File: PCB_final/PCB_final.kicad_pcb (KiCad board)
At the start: 4 copper layers, 90 x 95 mm, 115 parts, among them J1 02x30_Shift_Register_Connector, J2 02x30_ADC_Connector, J3 PicoPinSocketB, J4 PicoPinSocketA, U1 74HC595, U10 MCP6001T-I_OT, U2 74HC595, U3 74HC595, U4 74HC595, U5 74HC595, U6 74HC595, U7 74HC595, U8 MAX11643EEG, U9 MAX11643EEG

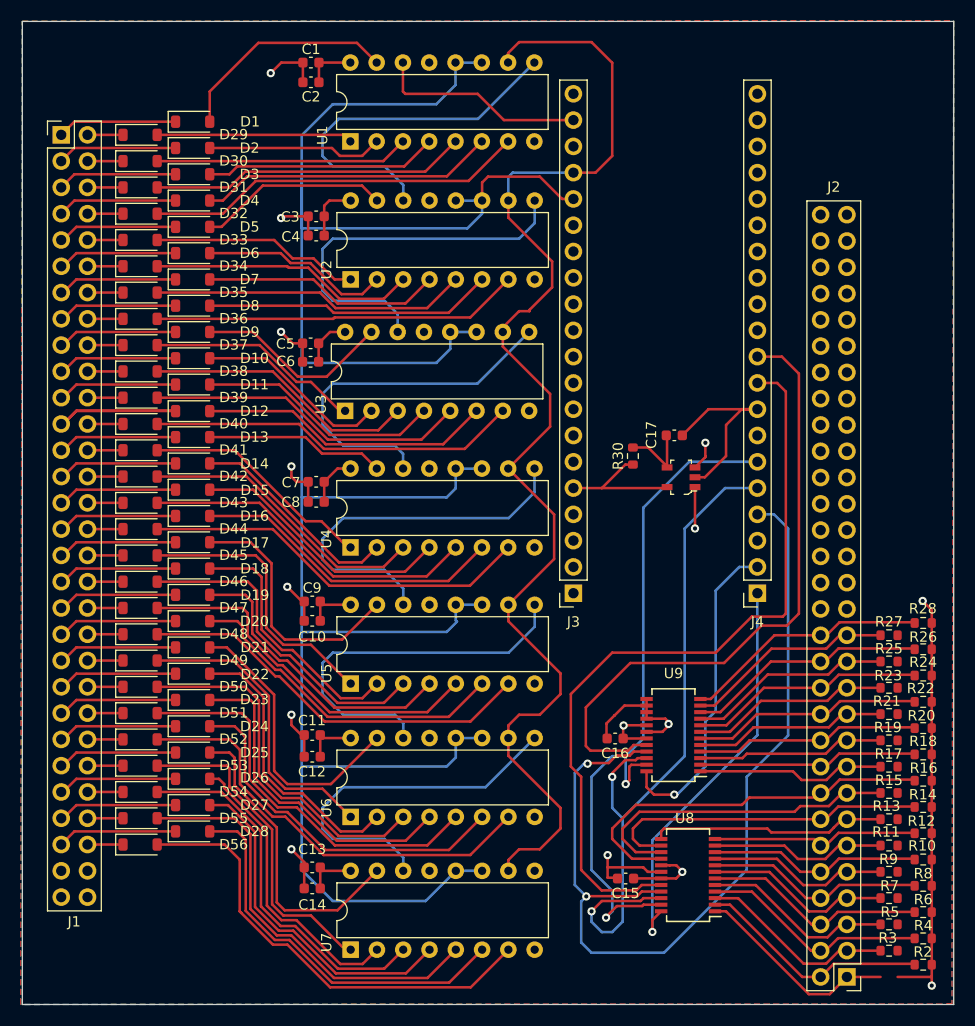
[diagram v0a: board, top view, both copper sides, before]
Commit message: Found naming errors with schematic and a few traces in PCB that weren't connected correctly. PCB now passes DRC with only a few warnings about silkscreen
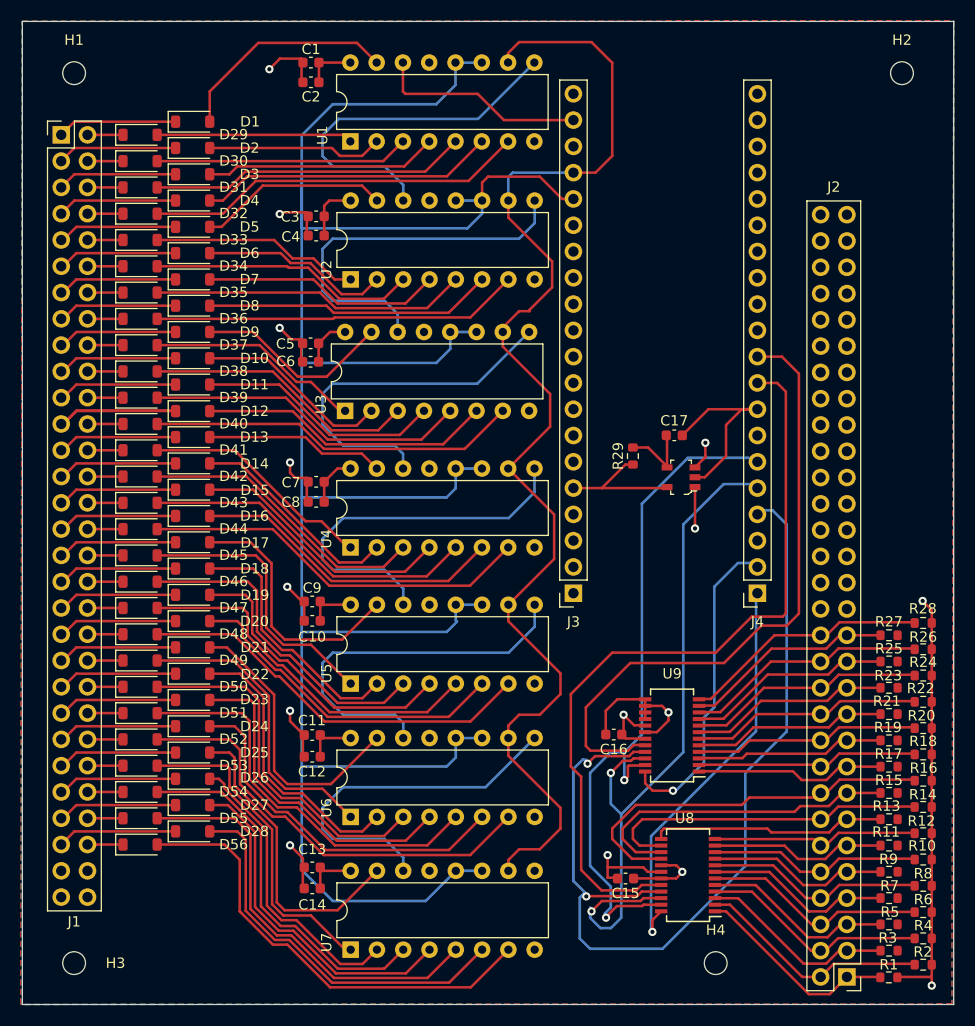
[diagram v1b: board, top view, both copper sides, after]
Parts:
- removed R30: 100k, Resistor_SMD:R_0603_1608Metric
- added H1: MountingHole, MountingHole:MountingHole_2.2mm_M2, F.Cu at (98.0, 65.0)
- added H2: MountingHole, MountingHole:MountingHole_2.2mm_M2, F.Cu at (178.0, 65.0)
- added H3: MountingHole, MountingHole:MountingHole_2.2mm_M2, F.Cu at (98.0, 151.0)
- added H4: MountingHole, MountingHole:MountingHole_2.2mm_M2, F.Cu at (160.0, 151.0)
- added R1: 100k, Resistor_SMD:R_0603_1608Metric, F.Cu at (176.7, 152.4)
- added R29: 100k, Resistor_SMD:R_0603_1608Metric, F.Cu at (152.0, 102.0)
- moved C16 0.40 mm to (150.2, 128.9)
- moved U9 0.14 mm to (155.8, 129.0)
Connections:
- R10 pad 1: /Interface Board/ADC_IN9 -> /Interface Board/ADC_IN10
- R11 pad 1: /Interface Board/ADC_IN10 -> /Interface Board/ADC_IN11
- R12 pad 1: /Interface Board/ADC_IN11 -> /Interface Board/ADC_IN12
- R13 pad 1: /Interface Board/ADC_IN12 -> /Interface Board/ADC_IN13
- R14 pad 1: /Interface Board/ADC_IN13 -> /Interface Board/ADC_IN14
- R15 pad 1: /Interface Board/ADC_IN14 -> /Interface Board/ADC_IN15
- R16 pad 1: /Interface Board/ADC_IN15 -> /Interface Board/ADC_IN16
- R17 pad 1: /Interface Board/ADC_IN16 -> /Interface Board/ADC_IN17
- R18 pad 1: /Interface Board/ADC_IN17 -> /Interface Board/ADC_IN18
- R19 pad 1: /Interface Board/ADC_IN18 -> /Interface Board/ADC_IN19
- R2 pad 1: /Interface Board/ADC_IN1 -> /Interface Board/ADC_IN2
- R20 pad 1: /Interface Board/ADC_IN19 -> /Interface Board/ADC_IN20
- R21 pad 1: /Interface Board/ADC_IN20 -> /Interface Board/ADC_IN21
- R22 pad 1: /Interface Board/ADC_IN21 -> /Interface Board/ADC_IN22
- R23 pad 1: /Interface Board/ADC_IN22 -> /Interface Board/ADC_IN23
- R24 pad 1: /Interface Board/ADC_IN23 -> /Interface Board/ADC_IN24
- R25 pad 1: /Interface Board/ADC_IN24 -> /Interface Board/ADC_IN25
- R26 pad 1: /Interface Board/ADC_IN25 -> /Interface Board/ADC_IN26
- R27 pad 1: /Interface Board/ADC_IN26 -> /Interface Board/ADC_IN27
- R28 pad 1: /Interface Board/ADC_IN27 -> /Interface Board/ADC_IN28
- R3 pad 1: /Interface Board/ADC_IN2 -> /Interface Board/ADC_IN3
- R4 pad 1: /Interface Board/ADC_IN3 -> /Interface Board/ADC_IN4
- R5 pad 1: /Interface Board/ADC_IN4 -> /Interface Board/ADC_IN5
- R6 pad 1: /Interface Board/ADC_IN5 -> /Interface Board/ADC_IN6
- R7 pad 1: /Interface Board/ADC_IN6 -> /Interface Board/ADC_IN7
- R8 pad 1: /Interface Board/ADC_IN7 -> /Interface Board/ADC_IN8
- R9 pad 1: /Interface Board/ADC_IN8 -> /Interface Board/ADC_IN9
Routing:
- net +3V3: track 55.0 -> 57.0 mm
- net GND: track 113.5 -> 115.1 mm
- net /Interface Board/SPI0_TX: track 70.1 -> 69.5 mm

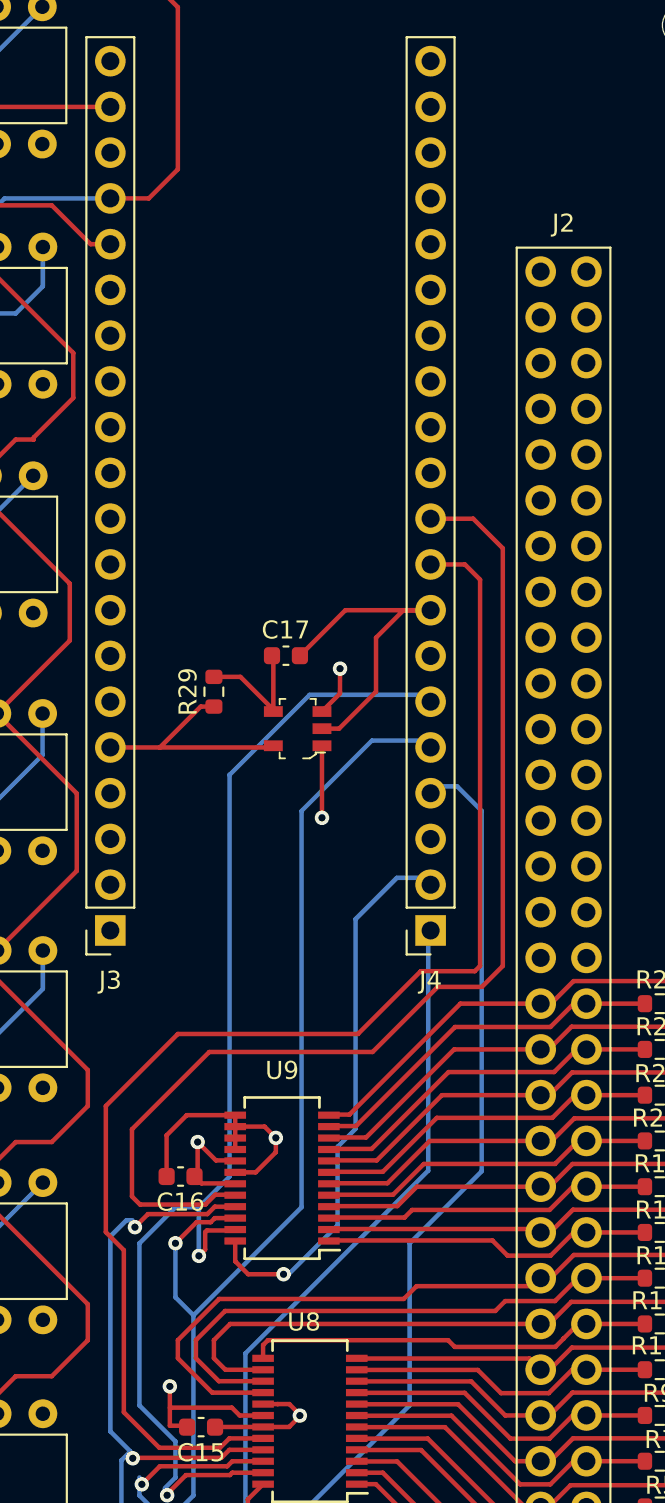
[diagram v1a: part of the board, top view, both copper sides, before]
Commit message: Removed filter from schematic and PCB. Adjusted tracings on PCB and schematic for ADC inputs so that each ADC has 14 inputs
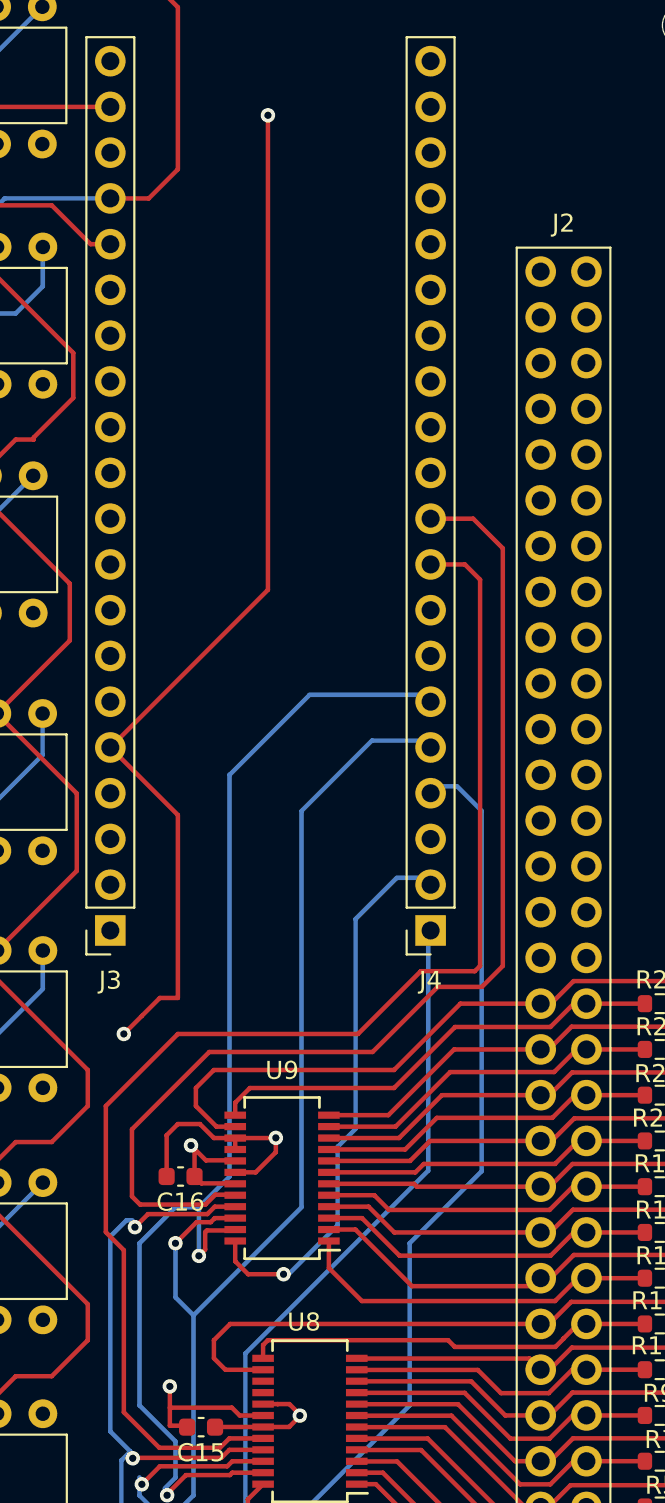
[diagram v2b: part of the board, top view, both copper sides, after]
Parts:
- removed C17: 0.1uF, Capacitor_SMD:C_0603_1608Metric
- removed R29: 100k, Resistor_SMD:R_0603_1608Metric
- removed U10: MCP6001T-I_OT, digikey-footprints:SOT-753
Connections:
- J3 pad 5: /Interface Board/3V3_Pico -> +3V3
- U8 pad 15: /Interface Board/ADC_IN15 -> GND
- U8 pad 16: /Interface Board/ADC_IN16 -> GND
- U9 pad 1: /Interface Board/ADC_IN17 -> /Interface Board/ADC_IN15
- U9 pad 10: /Interface Board/ADC_IN26 -> /Interface Board/ADC_IN24
- U9 pad 11: /Interface Board/ADC_IN27 -> /Interface Board/ADC_IN25
- U9 pad 12: /Interface Board/ADC_IN28 -> /Interface Board/ADC_IN26
- U9 pad 13: GND -> /Interface Board/ADC_IN27
- U9 pad 14: GND -> /Interface Board/ADC_IN28
- U9 pad 2: /Interface Board/ADC_IN18 -> /Interface Board/ADC_IN16
- U9 pad 3: /Interface Board/ADC_IN19 -> /Interface Board/ADC_IN17
- U9 pad 4: /Interface Board/ADC_IN20 -> /Interface Board/ADC_IN18
- U9 pad 5: /Interface Board/ADC_IN21 -> /Interface Board/ADC_IN19
- U9 pad 6: /Interface Board/ADC_IN22 -> /Interface Board/ADC_IN20
- U9 pad 7: /Interface Board/ADC_IN23 -> /Interface Board/ADC_IN21
- U9 pad 8: /Interface Board/ADC_IN24 -> /Interface Board/ADC_IN22
- U9 pad 9: /Interface Board/ADC_IN25 -> /Interface Board/ADC_IN23
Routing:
- net +3V3: track 57.0 -> 108.3 mm
- net GND: track 115.1 -> 94.9 mm
- net /Interface Board/ADC_IN16: track 37.7 -> 22.8 mm
- net /Interface Board/3V3_Pico: track 13.0 -> 0.00 mm
- net /Interface Board/ADC_IN15: track 31.6 -> 20.3 mm
- net /Interface Board/ADC_IN28: track 23.8 -> 34.3 mm
- net Net-(C17-Pad1): track 7.19 -> 0.00 mm
- net /Interface Board/ADC_IN27: track 20.2 -> 25.7 mm
- net /Interface Board/ADC_IN18: track 21.3 -> 22.2 mm
- net /Interface Board/ADC_IN17: track 18.3 -> 18.9 mm
